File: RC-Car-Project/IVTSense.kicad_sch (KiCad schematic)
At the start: 12 parts, among them U7 INA229AQDGSRQ1, U8 ADC082S021CIMM/NOPB

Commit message: Added Thermistor
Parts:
- R16, R21: value R -> 100kohm; MANUF_PN (none) -> RMCF0603FT100K
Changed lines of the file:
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@@
 			)
 		)
-		(property "Value" "R"
+		(property "Value" "100kohm"
 			(at 90.17 130.8099 0)
 			(effects
@@
 			)
 		)
-		(property "MANUF_PN" ""
+		(property "MANUF_PN" "RMCF0603FT100K"
 			(at 87.63 129.54 0)
 			(effects
@@
 			)
 		)
-		(property "Value" "R"
+		(property "Value" "100kohm"
 			(at 203.2 129.5399 0)
 			(effects
@@
 			)
 		)
-		(property "MANUF_PN" ""
+		(property "MANUF_PN" "RMCF0603FT100K"
 			(at 200.66 128.27 0)
 			(effects

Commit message: Fixed (AGAIN AGAIN)
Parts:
- renumbered C41 to C38, C42 to C39, C43 to C40, R16 to R41, R17 to R42, R18 to R43, R19 to R44, R20 to R45, R21 to R46, U7 to U6, U8 to U7
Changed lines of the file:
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@@
 		(dnp no)
 		(fields_autoplaced yes)
-		(property "Reference" "#PWR096"
+		(property "Reference" "#PWR0116"
 			(at 195.58 71.12 0)
 			(effects
@@
 			(project "RC-Car-Project"
 				(path "/ba870fd1-751d-4755-8e1a-1ea86ca9e2f6/9035ce50-cc35-47ce-85b3-06db8b07dac9"
-					(reference "#PWR096")
+					(reference "#PWR0116")
 					(unit 1)
 				)
@@
 		(dnp no)
 		(fields_autoplaced yes)
-		(property "Reference" "R16"
+		(property "Reference" "R41"
 			(at 90.17 128.2699 0)
 			(effects
@@
 			(project "RC-Car-Project"
 				(path "/ba870fd1-751d-4755-8e1a-1ea86ca9e2f6/9035ce50-cc35-47ce-85b3-06db8b07dac9"
-					(reference "R16")
+					(reference "R41")
 					(unit 1)
 				)
@@
 		(dnp no)
 		(fields_autoplaced yes)
-		(property "Reference" "R20"
+		(property "Reference" "R45"
 			(at 200.66 85.0899 90)
 			(effects
@@
 			(project "RC-Car-Project"
 				(path "/ba870fd1-751d-4755-8e1a-1ea86ca9e2f6/9035ce50-cc35-47ce-85b3-06db8b07dac9"
-					(reference "R20")
+					(reference "R45")
 					(unit 1)
 				)
@@
 		(dnp no)
 		(fields_autoplaced yes)
-		(property "Reference" "R19"
+		(property "Reference" "R44"
 			(at 186.69 85.09 90)
 			(effects
@@
 			(project "RC-Car-Project"
 				(path "/ba870fd1-751d-4755-8e1a-1ea86ca9e2f6/9035ce50-cc35-47ce-85b3-06db8b07dac9"
-					(reference "R19")
+					(reference "R44")
 					(unit 1)
 				)
@@
 		(dnp no)
 		(fields_autoplaced yes)
-		(property "Reference" "#PWR089"
+		(property "Reference" "#PWR0109"
 			(at 148.59 91.44 0)
 			(effects
@@
 			(project "RC-Car-Project"
 				(path "/ba870fd1-751d-4755-8e1a-1ea86ca9e2f6/9035ce50-cc35-47ce-85b3-06db8b07dac9"
-					(reference "#PWR089")
+					(reference "#PWR0109")
 					(unit 1)
 				)
@@
 		(dnp no)
 		(fields_autoplaced yes)
-		(property "Reference" "#PWR088"
+		(property "Reference" "#PWR0108"
 			(at 96.52 86.36 0)
 			(effects
@@
 			(project "RC-Car-Project"
 				(path "/ba870fd1-751d-4755-8e1a-1ea86ca9e2f6/9035ce50-cc35-47ce-85b3-06db8b07dac9"
-					(reference "#PWR088")
+					(reference "#PWR0108")
 					(unit 1)
 				)
@@
 		(dnp no)
 		(fields_autoplaced yes)
-		(property "Reference" "#PWR090"
+		(property "Reference" "#PWR0110"
 			(at 160.02 93.98 0)
 			(effects
@@
 			(project "RC-Car-Project"
 				(path "/ba870fd1-751d-4755-8e1a-1ea86ca9e2f6/9035ce50-cc35-47ce-85b3-06db8b07dac9"
-					(reference "#PWR090")
+					(reference "#PWR0110")
 					(unit 1)
 				)
@@
 		(dnp no)
 		(fields_autoplaced yes)
-		(property "Reference" "C43"
+		(property "Reference" "C40"
 			(at 189.23 132.0799 0)
 			(effects
@@
 			(project "RC-Car-Project"
 				(path "/ba870fd1-751d-4755-8e1a-1ea86ca9e2f6/9035ce50-cc35-47ce-85b3-06db8b07dac9"
-					(reference "C43")
+					(reference "C40")
 					(unit 1)
 				)
@@
 		(dnp no)
 		(fields_autoplaced yes)
-		(property "Reference" "#PWR091"
+		(property "Reference" "#PWR0111"
 			(at 156.21 110.49 0)
 			(effects
@@
 			(project "RC-Car-Project"
 				(path "/ba870fd1-751d-4755-8e1a-1ea86ca9e2f6/9035ce50-cc35-47ce-85b3-06db8b07dac9"
-					(reference "#PWR091")
+					(reference "#PWR0111")
 					(unit 1)
 				)
@@
 		(dnp no)
 		(fields_autoplaced yes)
-		(property "Reference" "#PWR095"
+		(property "Reference" "#PWR0115"
 			(at 184.15 129.54 0)
 			(effects
@@
 			(project "RC-Car-Project"
 				(path "/ba870fd1-751d-4755-8e1a-1ea86ca9e2f6/9035ce50-cc35-47ce-85b3-06db8b07dac9"
-					(reference "#PWR095")
+					(reference "#PWR0115")
 					(unit 1)
 				)
@@
 		(dnp no)
 		(fields_autoplaced yes)
-		(property "Reference" "#PWR093"
+		(property "Reference" "#PWR0113"
 			(at 170.18 127 0)
 			(effects
@@
 			(project "RC-Car-Project"
 				(path "/ba870fd1-751d-4755-8e1a-1ea86ca9e2f6/9035ce50-cc35-47ce-85b3-06db8b07dac9"
-					(reference "#PWR093")
+					(reference "#PWR0113")
 					(unit 1)
 				)
@@
 		(dnp no)
 		(fields_autoplaced yes)
-		(property "Reference" "R21"
+		(property "Reference" "R46"
 			(at 203.2 126.9999 0)
 			(effects
@@
 			(project "RC-Car-Project"
 				(path "/ba870fd1-751d-4755-8e1a-1ea86ca9e2f6/9035ce50-cc35-47ce-85b3-06db8b07dac9"
-					(reference "R21")
+					(reference "R46")
 					(unit 1)
 				)
@@
 		(dnp no)
 		(fields_autoplaced yes)
-		(property "Reference" "C42"
+		(property "Reference" "C39"
 			(at 172.72 85.0899 0)
 			(effects
@@
 			(project "RC-Car-Project"
 				(path "/ba870fd1-751d-4755-8e1a-1ea86ca9e2f6/9035ce50-cc35-47ce-85b3-06db8b07dac9"
-					(reference "C42")
+					(reference "C39")
 					(unit 1)
 				)
@@
 		(dnp no)
 		(fields_autoplaced yes)
-		(property "Reference" "#PWR097"
+		(property "Reference" "#PWR0117"
 			(at 195.58 111.76 0)
 			(effects
@@
 			(project "RC-Car-Project"
 				(path "/ba870fd1-751d-4755-8e1a-1ea86ca9e2f6/9035ce50-cc35-47ce-85b3-06db8b07dac9"
-					(reference "#PWR097")
+					(reference "#PWR0117")
 					(unit 1)
 				)
@@
 		(dnp no)
 		(fields_autoplaced yes)
-		(property "Reference" "U7"
+		(property "Reference" "U6"
 			(at 133.35 76.2 0)
 			(effects
@@
 			(project "RC-Car-Project"
 				(path "/ba870fd1-751d-4755-8e1a-1ea86ca9e2f6/9035ce50-cc35-47ce-85b3-06db8b07dac9"
-					(reference "U7")
+					(reference "U6")
 					(unit 1)
 				)
@@
 		(dnp no)
 		(fields_autoplaced yes)
-		(property "Reference" "#PWR094"
+		(property "Reference" "#PWR0114"
 			(at 185.42 143.51 0)
 			(effects
@@
 			(project "RC-Car-Project"
 				(path "/ba870fd1-751d-4755-8e1a-1ea86ca9e2f6/9035ce50-cc35-47ce-85b3-06db8b07dac9"
-					(reference "#PWR094")
+					(reference "#PWR0114")
 					(unit 1)
 				)
@@
 		(dnp no)
 		(fields_autoplaced yes)
-		(property "Reference" "#PWR092"
+		(property "Reference" "#PWR0112"
 			(at 156.21 96.52 0)
 			(effects
@@
 			(project "RC-Car-Project"
 				(path "/ba870fd1-751d-4755-8e1a-1ea86ca9e2f6/9035ce50-cc35-47ce-85b3-06db8b07dac9"
-					(reference "#PWR092")
+					(reference "#PWR0112")
 					(unit 1)
 				)
@@
 		(dnp no)
 		(fields_autoplaced yes)
-		(property "Reference" "R18"
+		(property "Reference" "R43"
 			(at 186.69 76.2 90)
 			(effects
@@
 			(project "RC-Car-Project"
 				(path "/ba870fd1-751d-4755-8e1a-1ea86ca9e2f6/9035ce50-cc35-47ce-85b3-06db8b07dac9"
-					(reference "R18")
+					(reference "R43")
 					(unit 1)
 				)
@@
 		(dnp no)
 		(fields_autoplaced yes)
-		(property "Reference" "U8"
+		(property "Reference" "U7"
 			(at 135.89 114.3 0)
 			(effects
@@
 			(project "RC-Car-Project"
 				(path "/ba870fd1-751d-4755-8e1a-1ea86ca9e2f6/9035ce50-cc35-47ce-85b3-06db8b07dac9"
-					(reference "U8")
+					(reference "U7")
 					(unit 1)
 				)
@@
 		(dnp no)
 		(fields_autoplaced yes)
-		(property "Reference" "#PWR098"
+		(property "Reference" "#PWR0118"
 			(at 200.66 138.43 0)
 			(effects
@@
 			(project "RC-Car-Project"
 				(path "/ba870fd1-751d-4755-8e1a-1ea86ca9e2f6/9035ce50-cc35-47ce-85b3-06db8b07dac9"
-					(reference "#PWR098")
+					(reference "#PWR0118")
 					(unit 1)
 				)
@@
 		(dnp no)
 		(fields_autoplaced yes)
-		(property "Reference" "R17"
+		(property "Reference" "R42"
 			(at 99.06 86.3599 0)
 			(effects
@@
 			(project "RC-Car-Project"
 				(path "/ba870fd1-751d-4755-8e1a-1ea86ca9e2f6/9035ce50-cc35-47ce-85b3-06db8b07dac9"
-					(reference "R17")
+					(reference "R42")
 					(unit 1)
 				)
@@
 		(dnp no)
 		(fields_autoplaced yes)
-		(property "Reference" "#PWR087"
+		(property "Reference" "#PWR0107"
 			(at 87.63 139.7 0)
 			(effects
@@
 			(project "RC-Car-Project"
 				(path "/ba870fd1-751d-4755-8e1a-1ea86ca9e2f6/9035ce50-cc35-47ce-85b3-06db8b07dac9"
-					(reference "#PWR087")
+					(reference "#PWR0107")
 					(unit 1)
 				)
@@
 		(dnp no)
 		(fields_autoplaced yes)
-		(property "Reference" "C41"
+		(property "Reference" "C38"
 			(at 160.02 99.0599 0)
 			(effects
@@
 			(project "RC-Car-Project"
 				(path "/ba870fd1-751d-4755-8e1a-1ea86ca9e2f6/9035ce50-cc35-47ce-85b3-06db8b07dac9"
-					(reference "C41")
-					(unit 1)
-				)
+					(reference "C38")
+					(unit 1)
+				)

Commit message: Most components speced
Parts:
- F1: MANUF_PN (none) -> SF-3812F6000T-2
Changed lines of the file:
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@@
+			)
+		)
+		(property "MANUF_PN" "SF-3812F6000T-2"
+			(at 195.58 105.41 0)
+			(effects
+				(font
+					(size 1.27 1.27)
+				)
+				(hide yes)
 			)
 		)

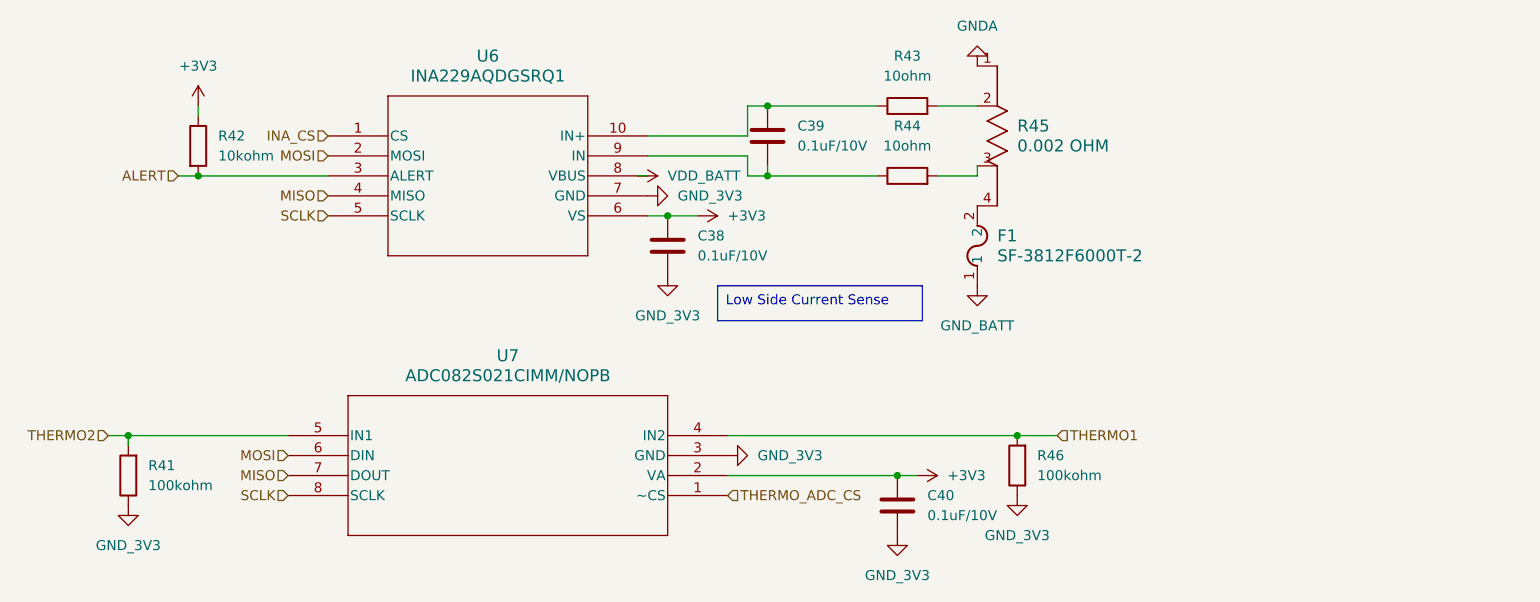
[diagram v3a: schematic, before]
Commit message: Finished BOM Drafts
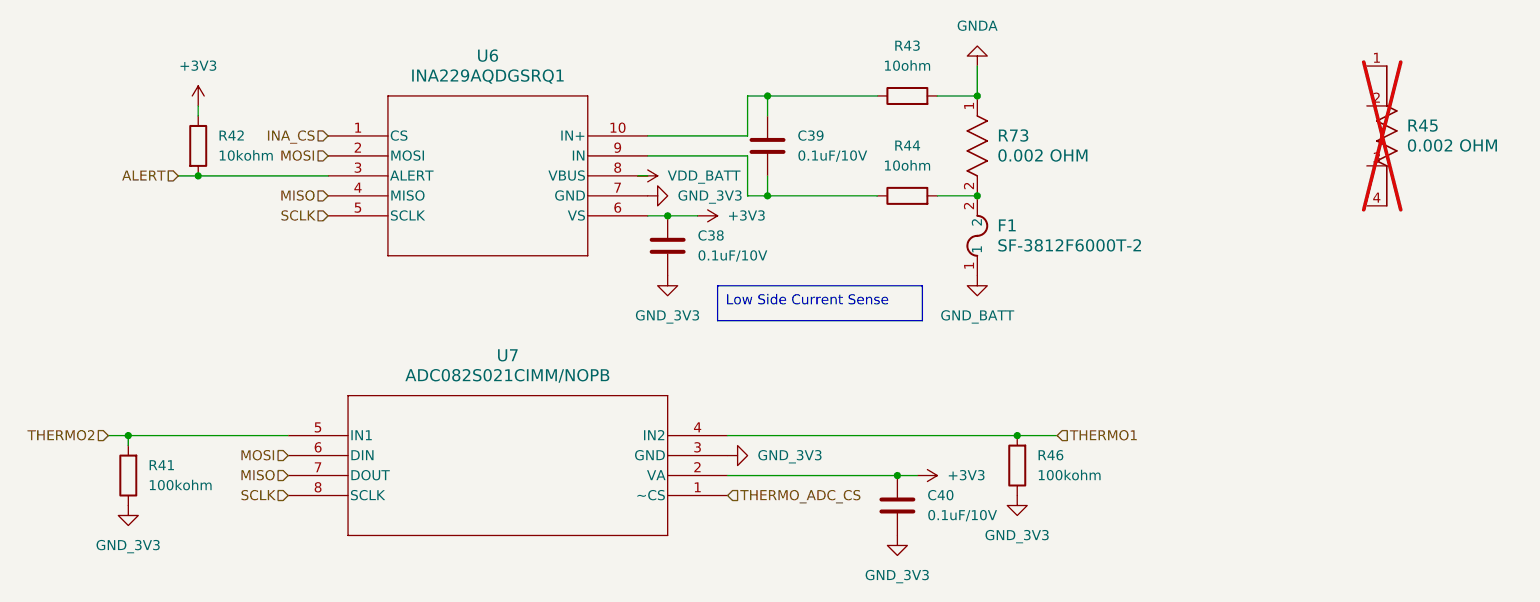
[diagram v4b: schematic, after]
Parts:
- added R73: 0.002 OHM, RES_WSLP5931_.002OHM_VIS, symbol WSLP59312L000FEA:WSLP59312L000FEA
- R45: now not fitted; now left out of the parts list
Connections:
- net GNDA: now also R43.2, R73.1; no longer R45.1
- net at R45.2: no longer R43.2
- net at R45.3: no longer R44.2
- net at R45.4: no longer F1.2
- new net: F1.2, R44.2, R73.2
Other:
- moved on the sheet: C39, F1, R43, R44
